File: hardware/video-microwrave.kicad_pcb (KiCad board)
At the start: 2 copper layers, 52.1 x 101.6 mm, 85 parts, among them J501 PJ301M-12, J502 PJ301M-12, J503 PJ301M-12, J504 PJ301M-12, J505 PJ301M-12, J506 PJ301M-12, J507 PJ301M-12, J508 PJ301M-12, P101 CONN_01X05, P102 CONN_01X05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

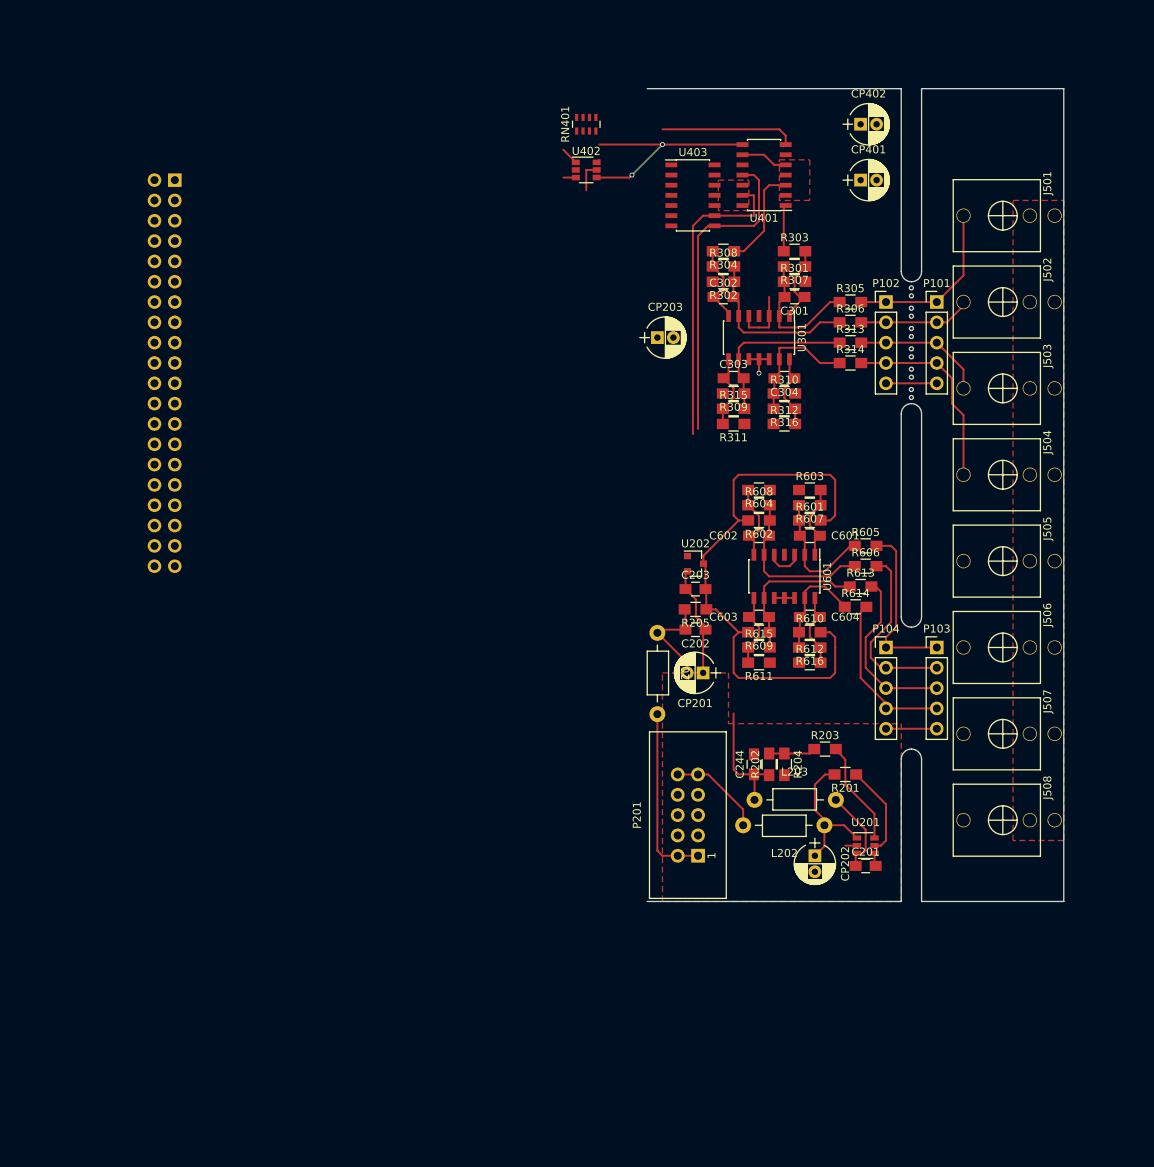
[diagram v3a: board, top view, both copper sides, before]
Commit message: nearly there. 3.3v power supply is missing though
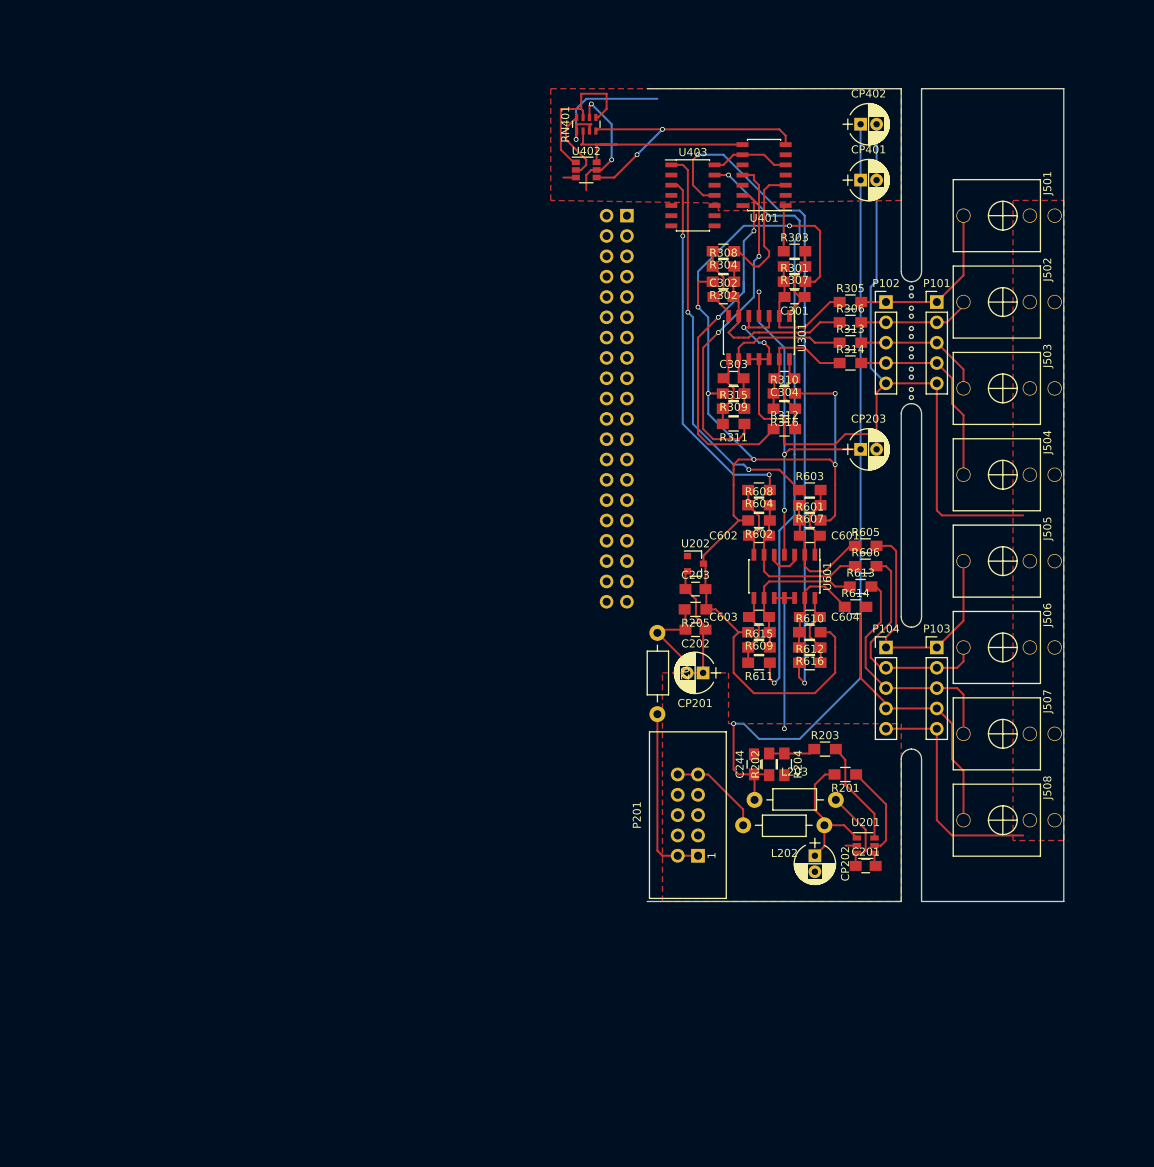
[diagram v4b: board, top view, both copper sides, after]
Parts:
- moved U101 56.7 mm to (118.1, 54.0)
- moved CP203 29.0 mm to (147.3, 83.2)
- moved R312 0.63 mm to (137.8, 80.6)
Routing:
- net +5V: track 15.0 -> 168.9 mm, vias 0 -> 5
- net Earth: track 54.0 -> 178.0 mm, vias 1 -> 2
- net /buffered_8: track 0.00 -> 85.0 mm, vias 0 -> 2
- net /buffers 1-4/-5V: track 72.1 -> 150.2 mm, vias 0 -> 6
- net /buffered_7: track 0.00 -> 74.9 mm, vias 0 -> 2
- net /buffered_5: track 0.00 -> 51.1 mm, vias 0 -> 2
- net /buffered_6: track 0.00 -> 46.3 mm, vias 0 -> 2
- net +3V3: track 3.80 -> 21.6 mm
- net (no net): track 0.00 -> 15.9 mm, vias 0 -> 1
- net /cv8_raw: track 20.7 -> 36.0 mm
- net /cv5_raw: track 21.7 -> 33.8 mm
- net /I2C_clock: track 3.84 -> 15.7 mm, vias 0 -> 2
- net /adc/SDA_5V: track 26.8 -> 36.0 mm
- net /I2C_data: track 0.00 -> 9.10 mm
- net /cv7_raw: track 21.7 -> 30.3 mm
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
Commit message: looking pretty ugly, but very close
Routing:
- net /I2C_data: track 9.10 -> 30.3 mm
- net /I2C_clock: track 15.7 -> 31.0 mm, vias 2 -> 3
- net +5V: track 168.9 -> 173.6 mm, vias 5 -> 7
- added copper zone on B.Cu, net +5V

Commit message: still some unconnected pads, but might be good enough for a prototype. marked rev1
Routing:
- net Earth: track 178.0 -> 197.4 mm
- net (no net): track 15.9 -> 0.00 mm, vias 1 -> 0
- net /adc/SDA_5V: track 36.0 -> 47.7 mm
- net +5V: track 173.6 -> 179.2 mm, vias 7 -> 9
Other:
- board size 52.1 x 101.6 mm -> 66 x 101.6 mm
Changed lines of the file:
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@@
   (general
     (links 210)
-    (no_connects 28)
+    (no_connects 9)
     (area 120.574999 38.024999 172.795001 139.775001)
     (thickness 1.6)
-    (drawings 19)
-    (tracks 589)
+    (drawings 27)
+    (tracks 605)
     (zones 0)
     (modules 85)
@@
   )
   (page A4)
+  (title_block
+    (title "Video MicroWrave")
+    (date 2018-11-14)
+    (rev 1)
+    (company RGBk.org)
+    (comment 1 "it's ugly, but probably works")
+  )
   (layers
     (0 F.Cu signal)
@@
       (net 23 "Net-(C201-Pad1)"))
   )
+  (gr_line (start 119.38 139.7) (end 120.65 139.7) (angle 90) (layer Edge.Cuts) (width 0.15))
+  (gr_line (start 119.38 112.395) (end 119.38 139.7) (angle 90) (layer Edge.Cuts) (width 0.15))
+  (gr_arc (start 118.745 112.395) (end 118.745 111.76) (angle 90) (layer Edge.Cuts) (width 0.15))
+  (gr_line (start 112.395 105.41) (end 118.745 111.76) (angle 90) (layer Edge.Cuts) (width 0.15))
+  (gr_line (start 112.395 60.325) (end 112.395 105.41) (angle 90) (layer Edge.Cuts) (width 0.15))
+  (gr_line (start 106.68 54.61) (end 112.395 60.325) (angle 90) (layer Edge.Cuts) (width 0.15))
+  (gr_line (start 106.68 38.1) (end 106.68 54.61) (angle 90) (layer Edge.Cuts) (width 0.15))
+  (gr_line (start 120.65 38.1) (end 106.68 38.1) (angle 90) (layer Edge.Cuts) (width 0.15))
   (gr_line (start 152.4 78.74) (end 152.4 104.14) (angle 90) (layer Edge.Cuts) (width 0.15))
   (gr_line (start 154.94 104.14) (end 154.94 78.74) (angle 90) (layer Edge.Cuts) (width 0.15))
@@
   (gr_line (start 152.4 139.7) (end 120.65 139.7) (angle 90) (layer Edge.Cuts) (width 0.15))
   (gr_line (start 120.65 38.1) (end 152.4 38.1) (angle 90) (layer Edge.Cuts) (width 0.15))
-  (segment (start 137.795 102.235) (end 137.795 118.11) (width 0.25) (layer B.Cu) (net 0))
-  (via (at 137.795 118.11) (size 0.6) (drill 0.4) (layers F.Cu B.Cu) (net 0))
   (segment (start 137.815 64.135) (end 137.815 62.33) (width 0.25) (layer F.Cu) (net 1))
   (segment (start 137.815 62.33) (end 137.715 62.23) (width 0.25) (layer F.Cu) (net 1))
@@
   (segment (start 138.43 73.68) (end 139.045 74.295) (width 0.25) (layer F.Cu) (net 8))
   (segment (start 138.43 71.915) (end 138.43 72.41) (width 0.25) (layer F.Cu) (net 8))
+  (segment (start 137.955 48.895) (end 140.97 48.895) (width 0.25) (layer F.Cu) (net 9))
+  (segment (start 149.32 40.735) (end 149.32 42.545) (width 0.25) (layer F.Cu) (net 9))
+  (segment (start 148.59 40.005) (end 149.32 40.735) (width 0.25) (layer F.Cu) (net 9))
+  (segment (start 146.05 40.005) (end 148.59 40.005) (width 0.25) (layer F.Cu) (net 9))
+  (segment (start 144.145 41.91) (end 146.05 40.005) (width 0.25) (layer F.Cu) (net 9))
+  (segment (start 144.145 45.72) (end 144.145 41.91) (width 0.25) (layer F.Cu) (net 9))
+  (segment (start 140.97 48.895) (end 144.145 45.72) (width 0.25) (layer F.Cu) (net 9))
   (segment (start 133.35 67.945) (end 132.715 67.945) (width 0.25) (layer F.Cu) (net 9))
   (segment (start 135.89 70.485) (end 135.89 71.915) (width 0.25) (layer F.Cu) (net 9))
@@
   (segment (start 136.525 47.625) (end 137.955 47.625) (width 0.25) (layer F.Cu) (net 9) (status 30))
   (segment (start 135.255 46.355) (end 136.525 47.625) (width 0.25) (layer F.Cu) (net 9) (status 20))
+  (segment (start 132.555 47.625) (end 133.985 47.625) (width 0.25) (layer F.Cu) (net 10))
+  (segment (start 134.62 48.26) (end 135.255 48.895) (width 0.25) (layer B.Cu) (net 10))
+  (via (at 134.62 48.26) (size 0.6) (drill 0.4) (layers F.Cu B.Cu) (net 10))
+  (segment (start 133.985 47.625) (end 134.62 48.26) (width 0.25) (layer F.Cu) (net 10))
+  (segment (start 137.955 46.355) (end 139.7 46.355) (width 0.25) (layer F.Cu) (net 10))
+  (segment (start 139.7 46.355) (end 140.335 46.355) (width 0.25) (layer B.Cu) (net 10))
+  (via (at 139.7 46.355) (size 0.6) (drill 0.4) (layers F.Cu B.Cu) (net 10))
   (segment (start 130.81 53.975) (end 130.81 53.34) (width 0.25) (layer B.Cu) (net 10))
   (via (at 130.81 53.975) (size 0.6) (drill 0.4) (layers F.Cu B.Cu) (net 10))
@@
   (segment (start 132.555 45.085) (end 116.84 45.085) (width 0.25) (layer F.Cu) (net 20) (status 10))
   (segment (start 116.84 45.085) (end 114.65 45.085) (width 0.25) (layer F.Cu) (net 20))
+  (segment (start 123.665 55.245) (end 121.92 55.245) (width 0.25) (layer F.Cu) (net 21))
+  (segment (start 121.285 48.26) (end 119.38 46.355) (width 0.25) (layer F.Cu) (net 21))
+  (segment (start 121.285 54.61) (end 121.285 48.26) (width 0.25) (layer F.Cu) (net 21))
+  (segment (start 121.92 55.245) (end 121.285 54.61) (width 0.25) (layer F.Cu) (net 21))
   (segment (start 137.955 43.975) (end 137.16 43.18) (width 0.25) (layer F.Cu) (net 21) (status 10))
   (segment (start 122.555 43.18) (end 114.445 43.18) (width 0.25) (layer F.Cu) (net 21))
@@
       (pts
         (xy 152.4 52.07) (xy 133.35 52.346087) (xy 133.35 53.34) (xy 129.54 53.34) (xy 129.54 52.401304)
-        (xy 108.585 52.07) (xy 108.585 38.1) (xy 152.4 38.1)
+        (xy 120.65 52.260751) (xy 120.65 94.615) (xy 143.51 94.615) (xy 143.51 107.315) (xy 120.015 107.315)
+        (xy 120.015 104.775) (xy 113.03 104.775) (xy 113.03 52.140277) (xy 108.585 52.07) (xy 108.585 38.1)
+        (xy 152.4 38.1)
       )
     )
